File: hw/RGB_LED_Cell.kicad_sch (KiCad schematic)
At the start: 4 parts

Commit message: updated RGB Led Cell
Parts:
- renumbered D49 to D7, R145 to R19, R146 to R20, R147 to R21

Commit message: updated sheets information
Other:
- company: (none) -> Qingdao IotPi Information Technology Ltd.,
- title: (none) -> KiCad 2023 Shen Zhen Badge

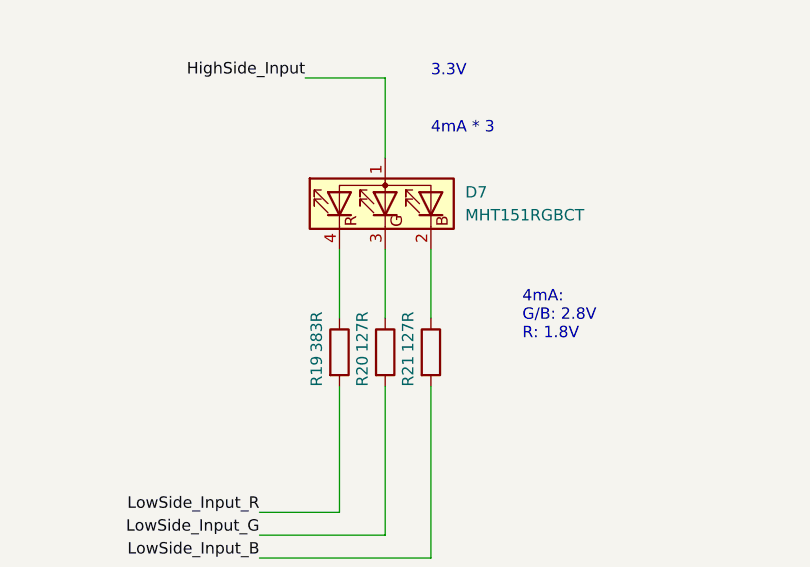
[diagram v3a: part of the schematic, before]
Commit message: unknown reason caused updated reference
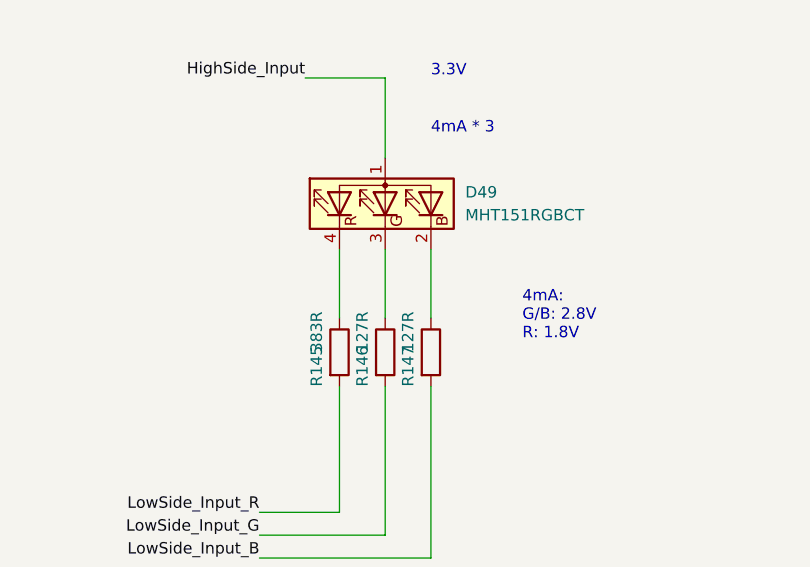
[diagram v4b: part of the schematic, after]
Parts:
- renumbered D7 to D49, R19 to R145, R20 to R146, R21 to R147
